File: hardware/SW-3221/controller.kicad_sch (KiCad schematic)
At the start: 31 parts, among them J2 USB_B_Micro, J3 ESPFlash, J4 JTAG, J5 I2C, Q1 S8050, Q2 S8050, SW1 RESET, SW2 BOOT, U1 CP2102N-A02-GQFN24, U2 ESP32-WROOM-32D

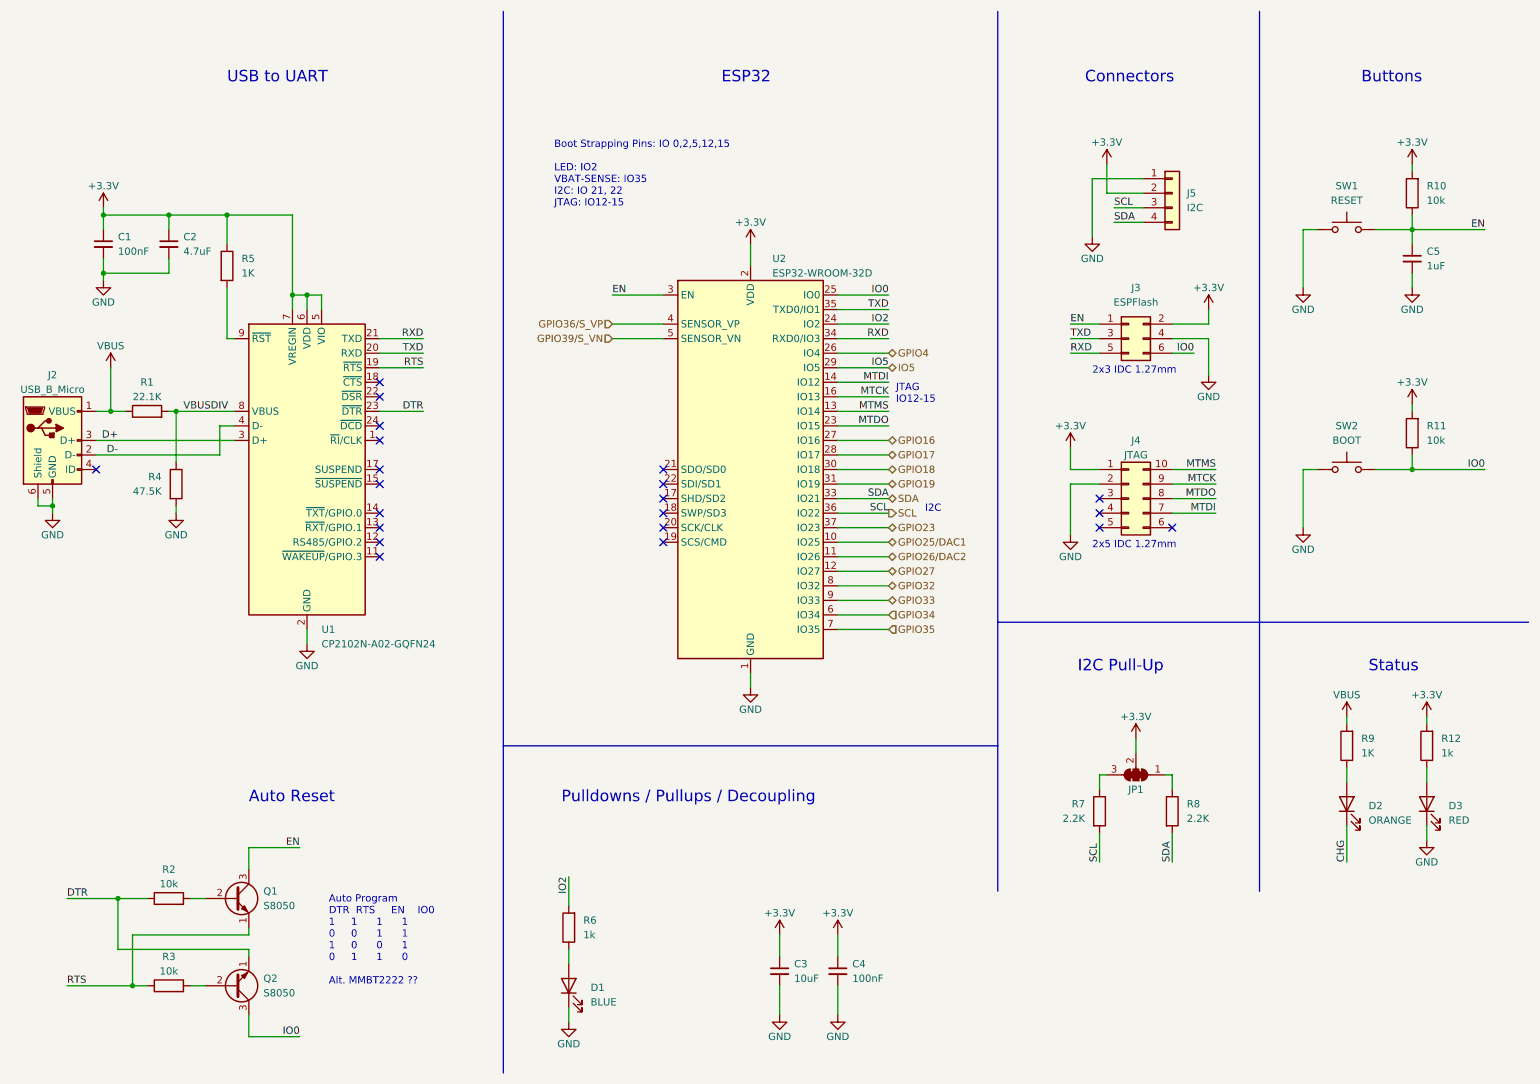
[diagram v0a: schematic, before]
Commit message: use io5 for encoder switch
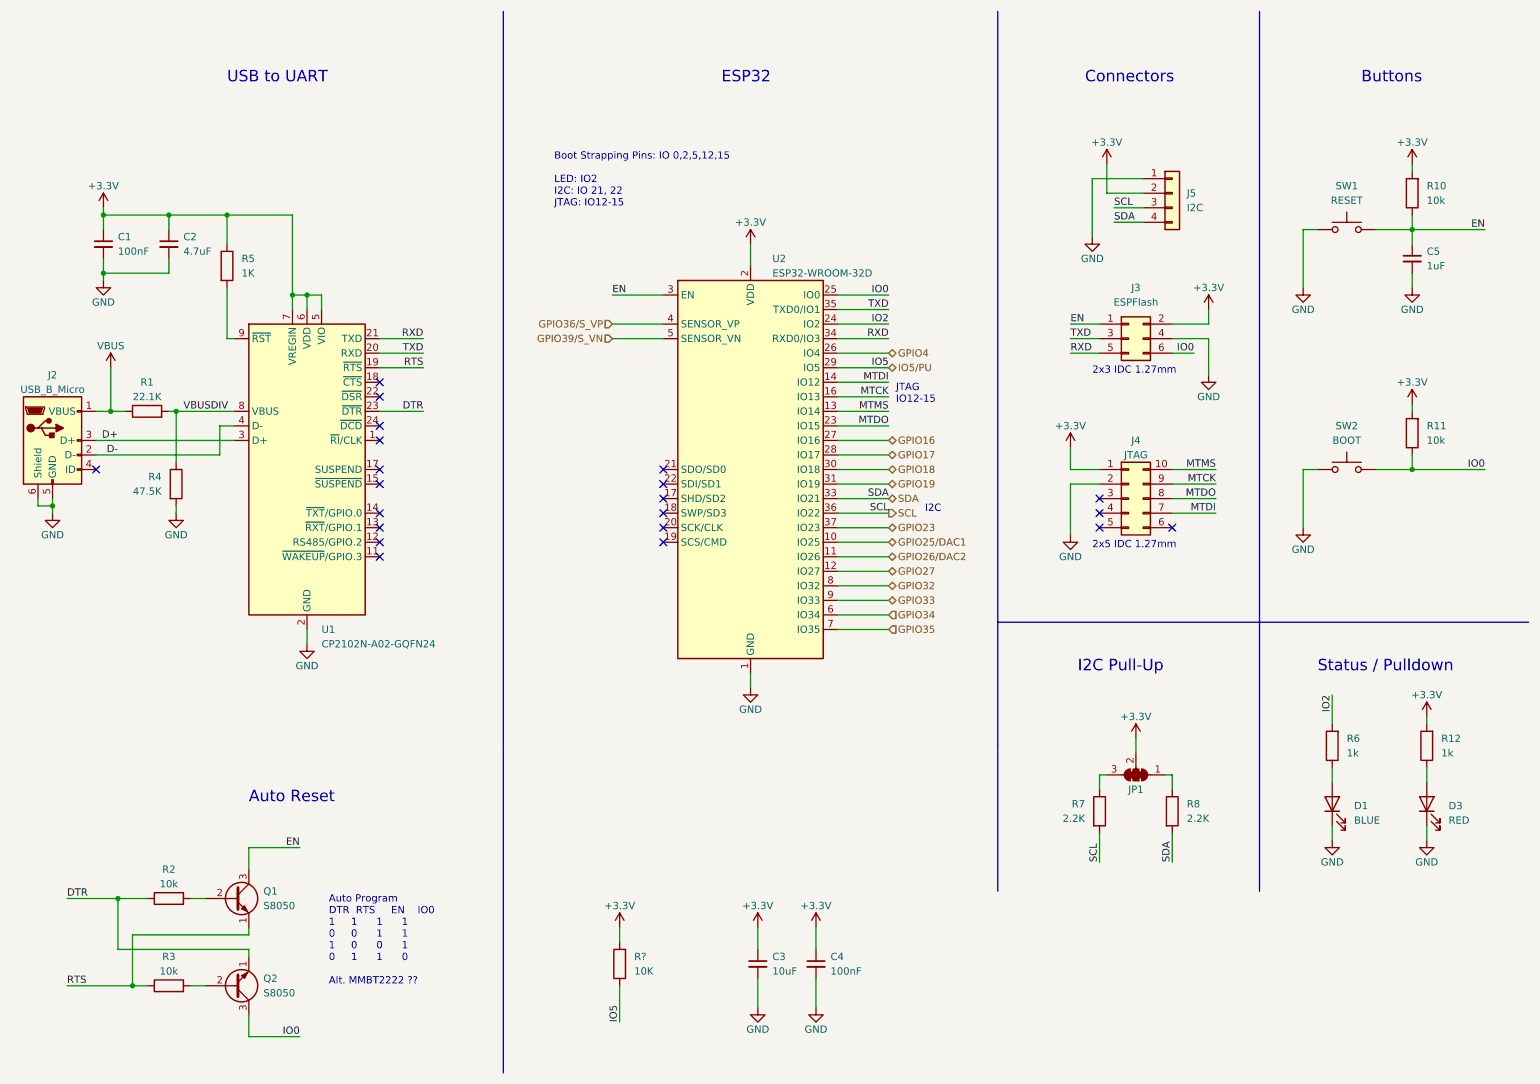
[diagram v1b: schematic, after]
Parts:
- removed D2: ORANGE, LED_SMD:LED_0805_2012Metric, symbol Device:LED
- removed R9: 1K, Resistor_SMD:R_0603_1608Metric, symbol Device:R
- added R?: 10K, Resistor_SMD:R_0603_1608Metric, symbol Device:R
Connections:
- net +3V3: now also R?.2
- net IO5 renamed IO5/PU
- net IO5/PU: now also R?.1
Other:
- note added: "Boot Strapping Pins: IO 0,2,5,12,15 LED: IO2 I2C: IO 21, 22 JTAG: IO12-15"
- note added: "Status / Pulldown"
- note removed: "Boot Strapping Pins: IO 0,2,5,12,15 LED: IO2 VBAT-SENSE: IO35 I2C: IO 21, 22 JTAG: IO12-15"
- note removed: "Pulldowns / Pullups / Decoupling"
- note removed: "Status"
- moved on the sheet: C3, C4, D1, R6
